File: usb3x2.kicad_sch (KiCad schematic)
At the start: 102 parts

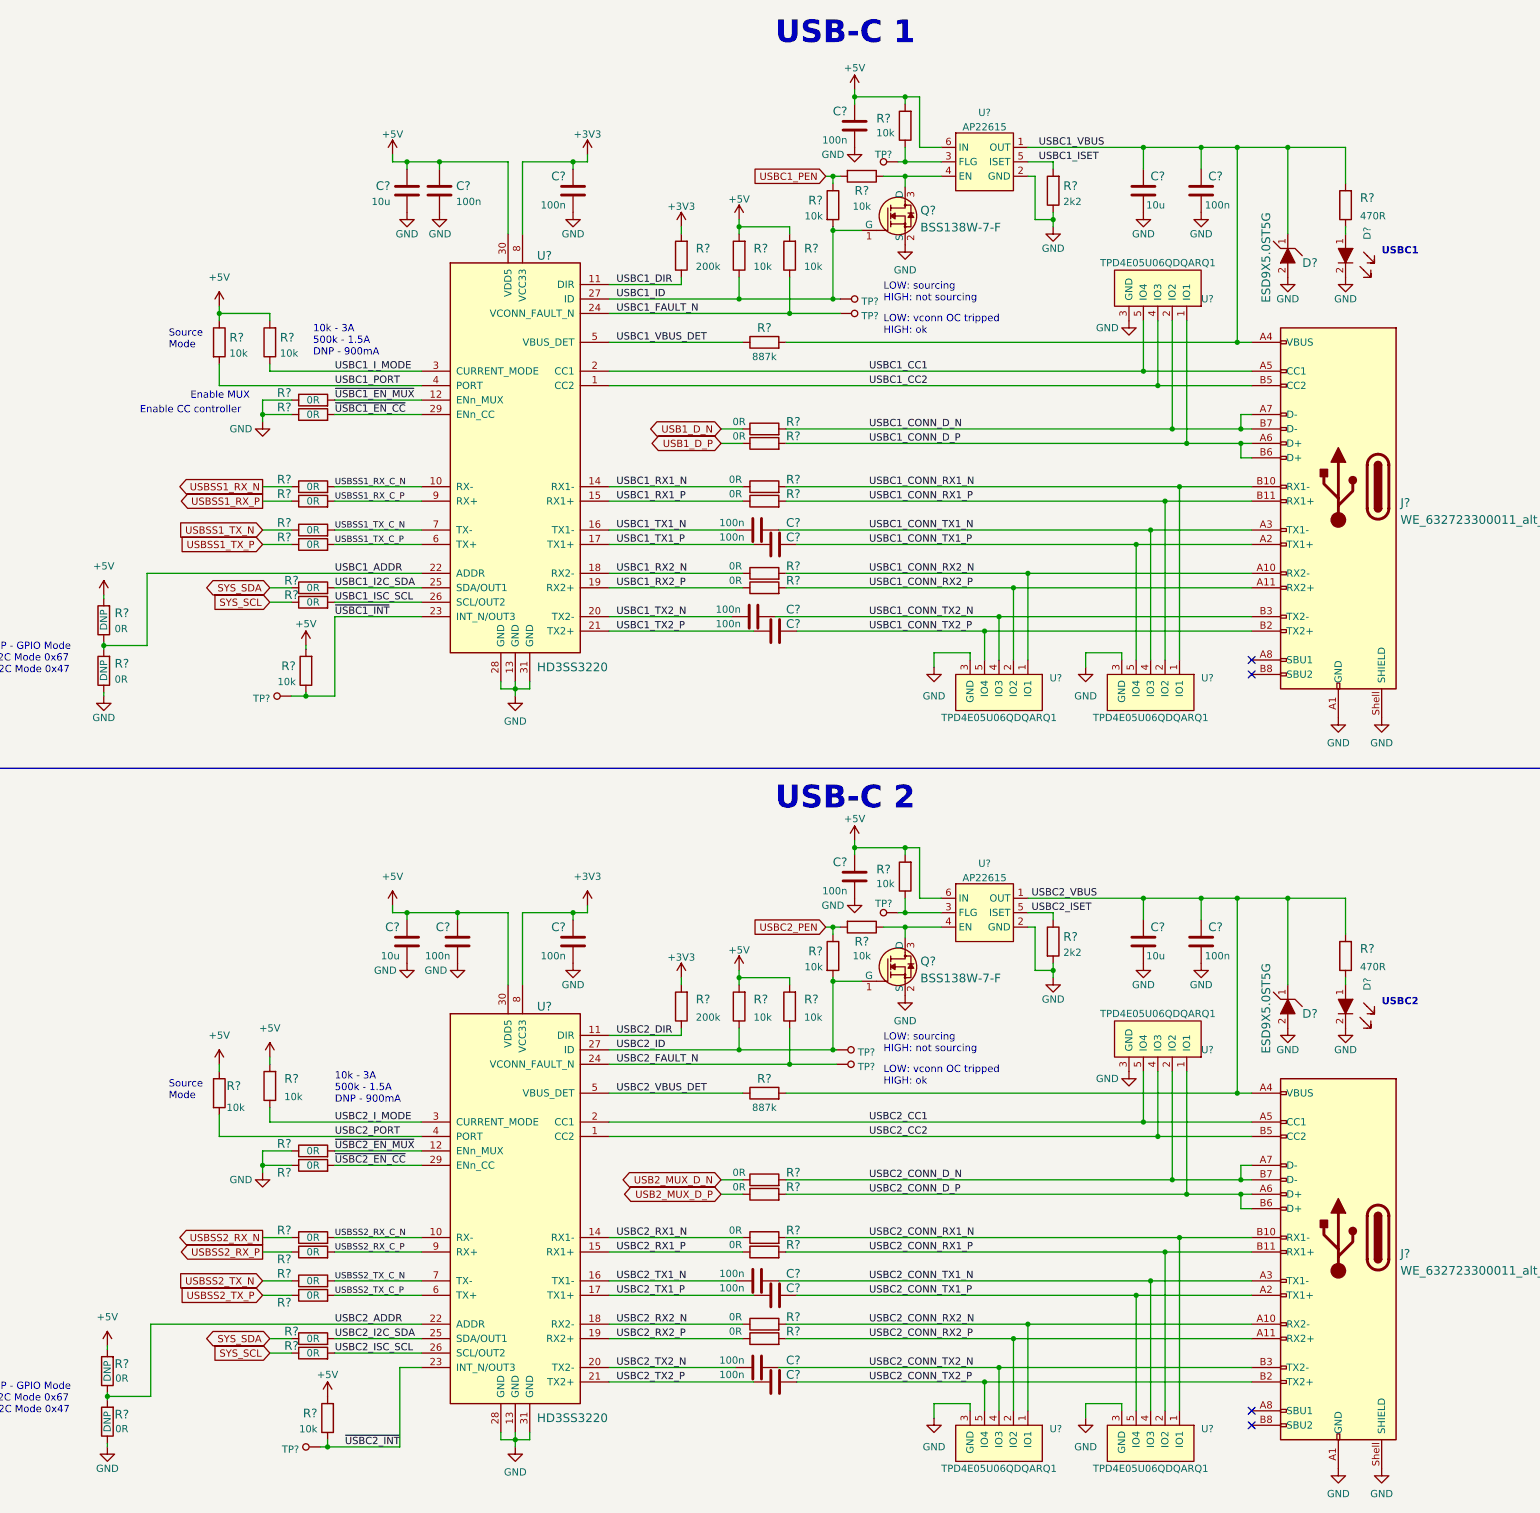
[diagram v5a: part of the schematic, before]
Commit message: Added soft power button and annotated schematic
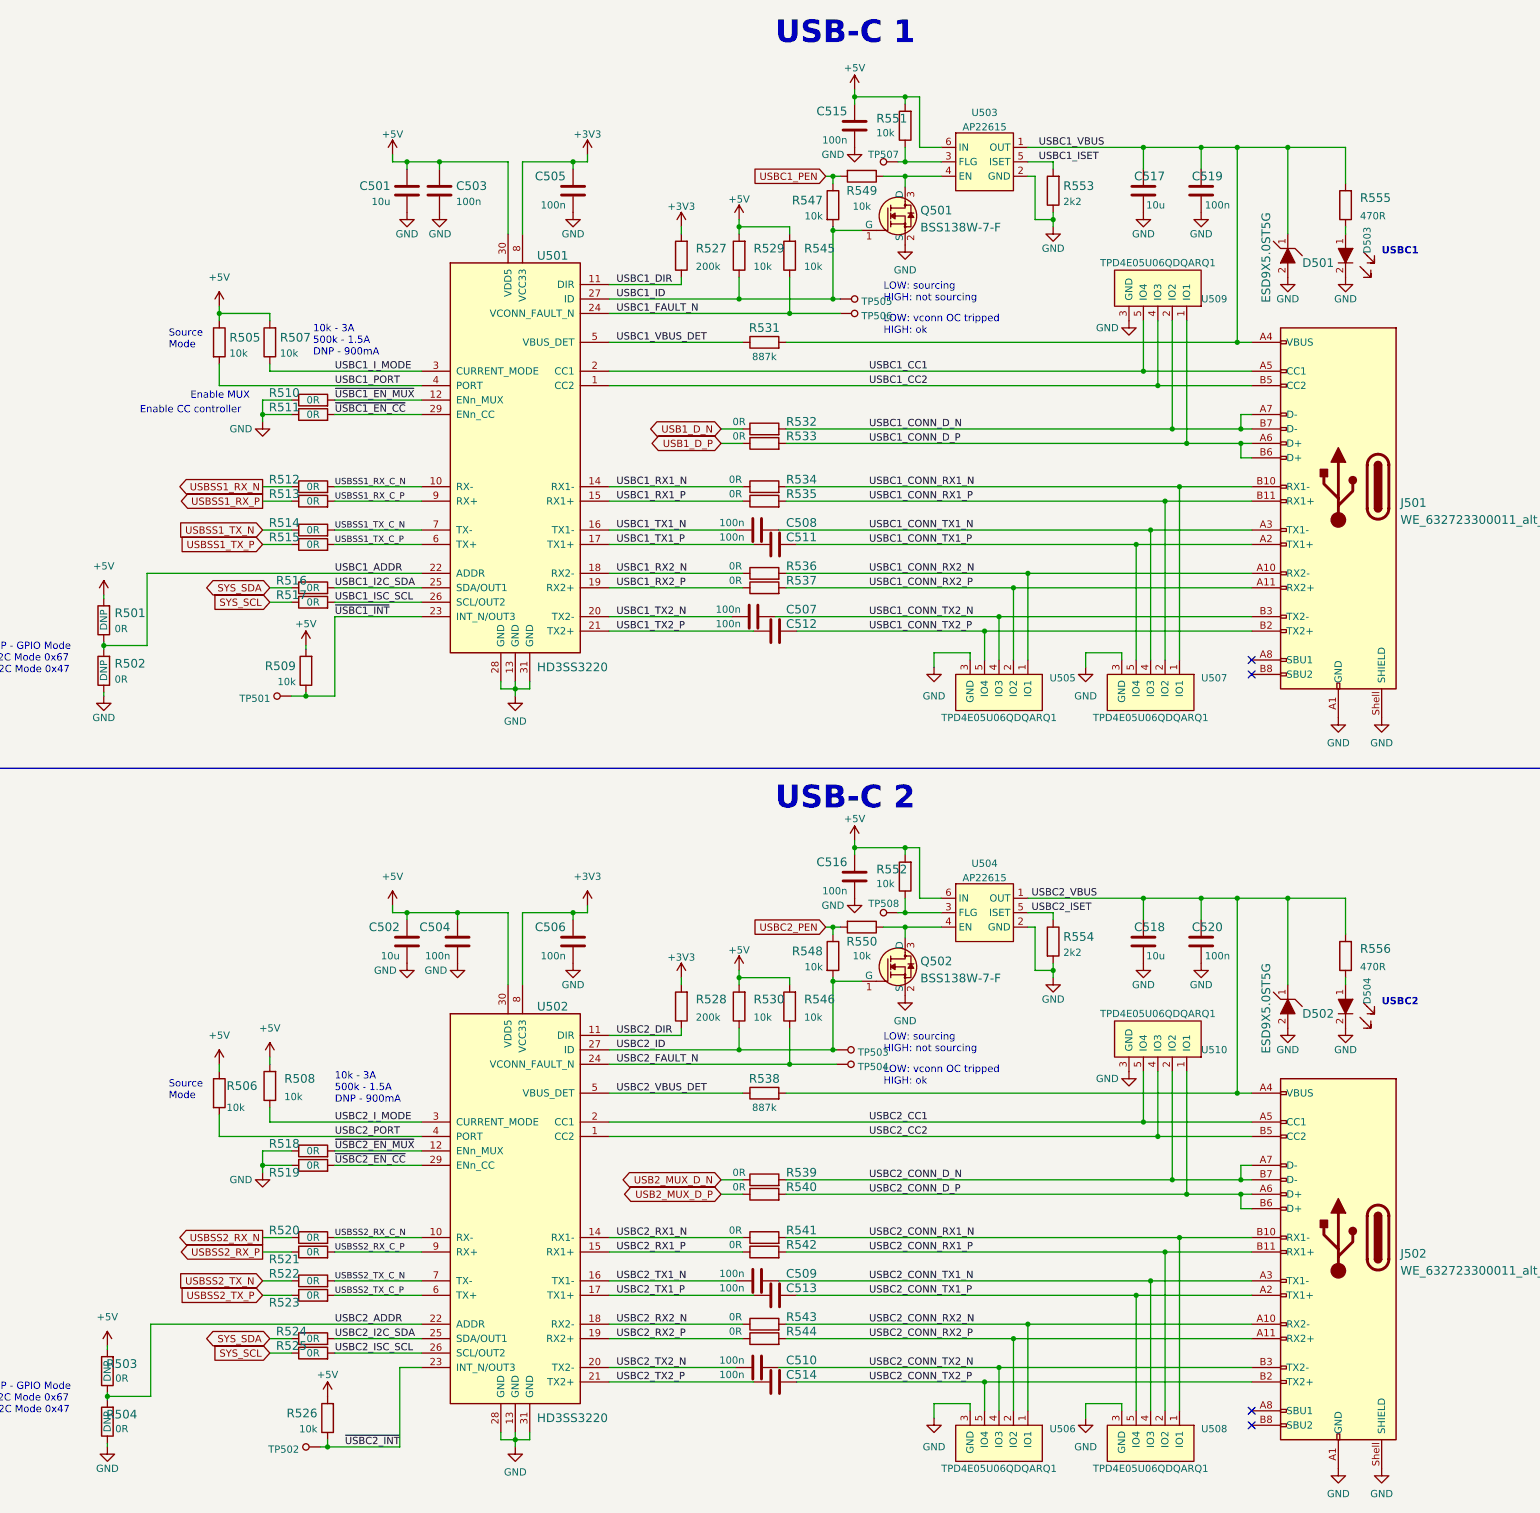
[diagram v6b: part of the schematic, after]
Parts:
- gave numbers to parts that had none: 102

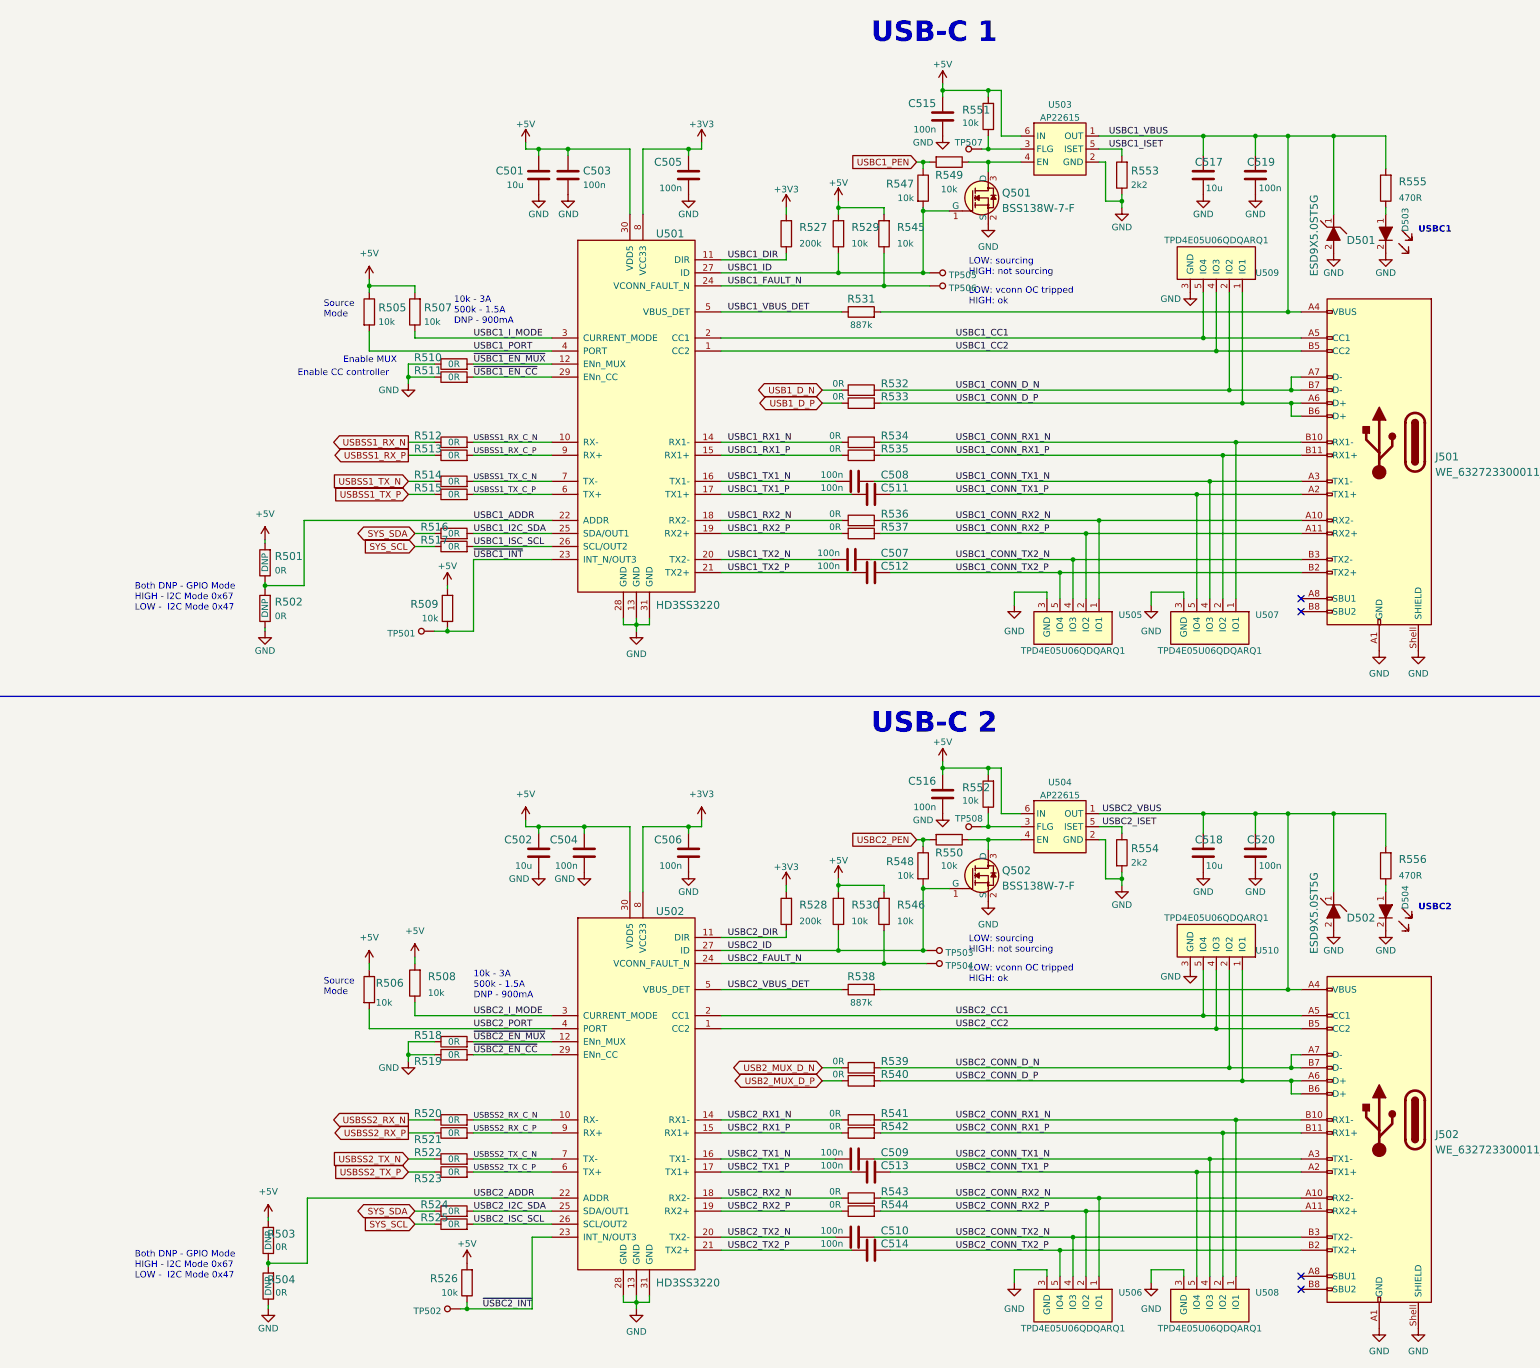
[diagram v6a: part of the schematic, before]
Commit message: Readability improvements
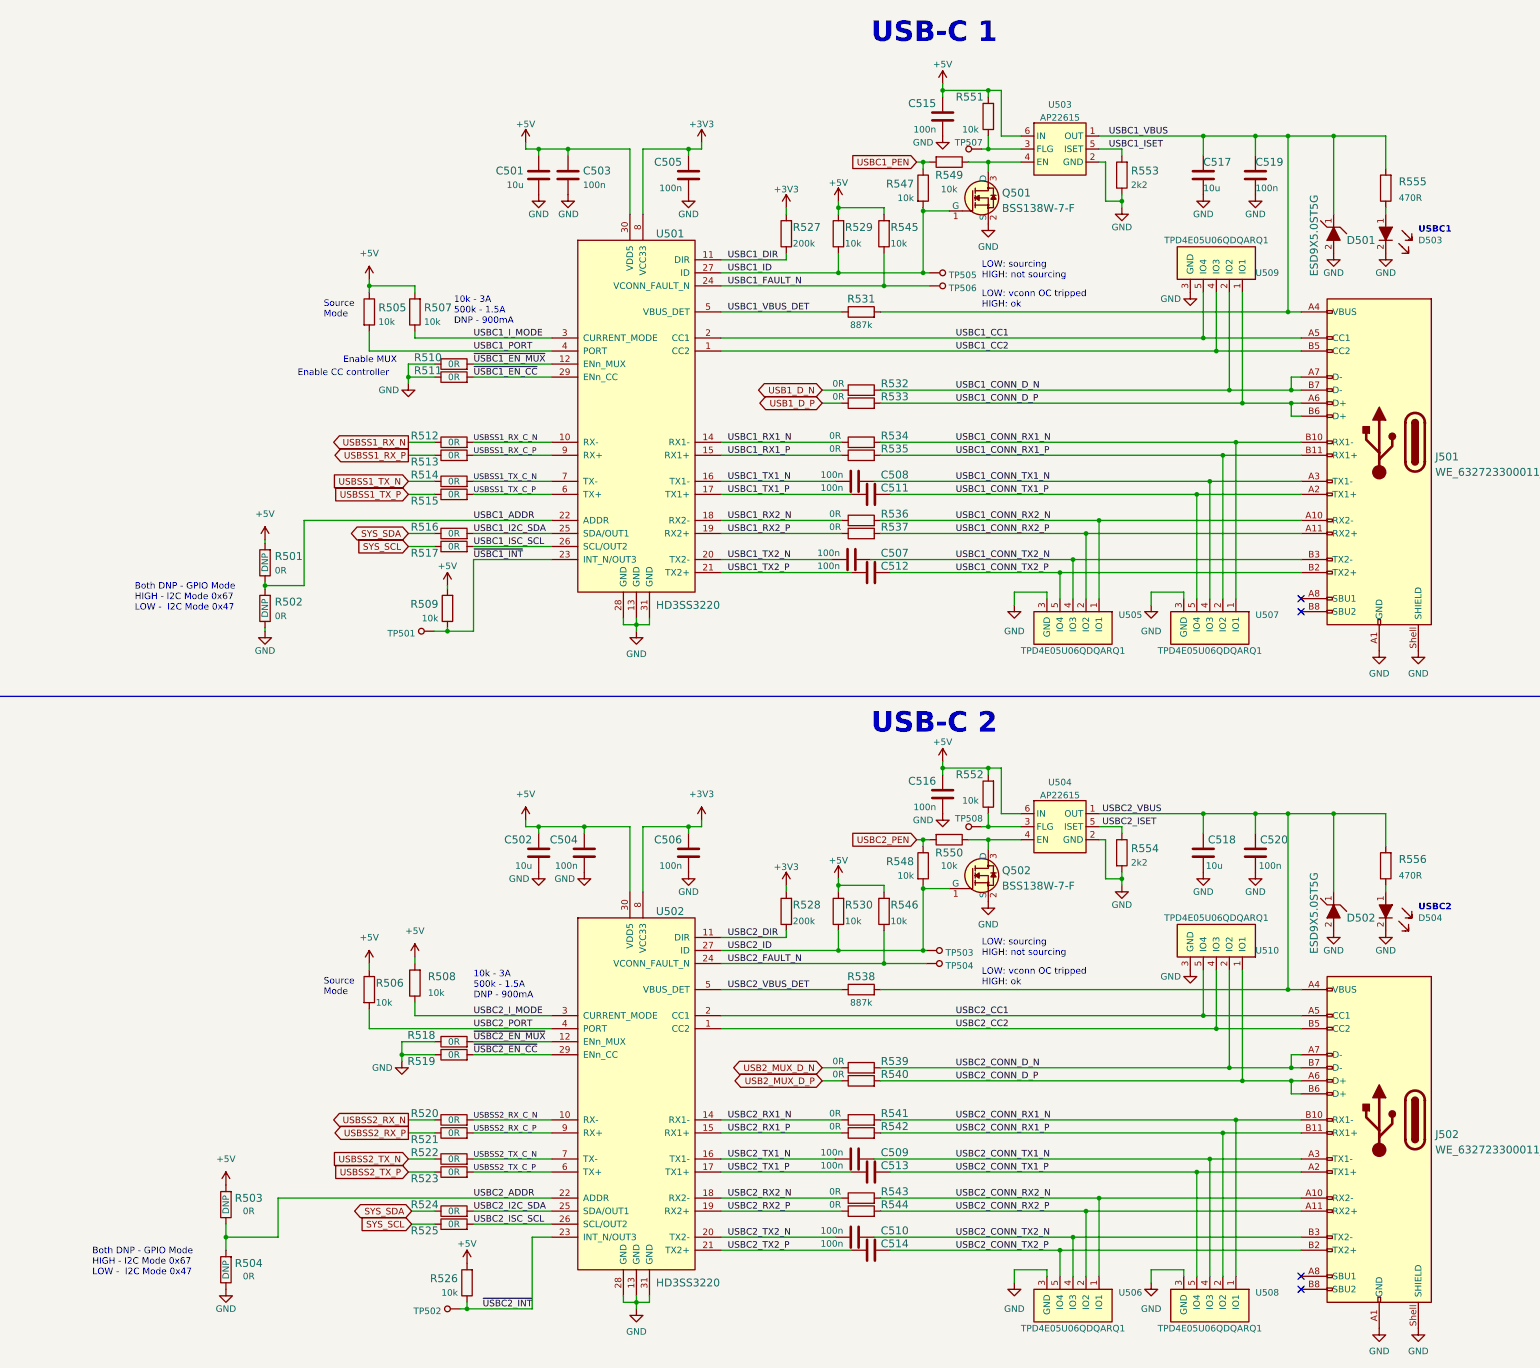
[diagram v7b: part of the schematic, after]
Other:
- moved on the sheet: R503, R504
